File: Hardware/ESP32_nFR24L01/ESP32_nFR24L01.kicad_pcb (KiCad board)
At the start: 2 copper layers, 4 parts, among them J1 Conn_01x02_Female, U1 ESP32_DevKit_V1_DOIT, U2 NRF24L01_Breakout, U3 LM2596-Baja

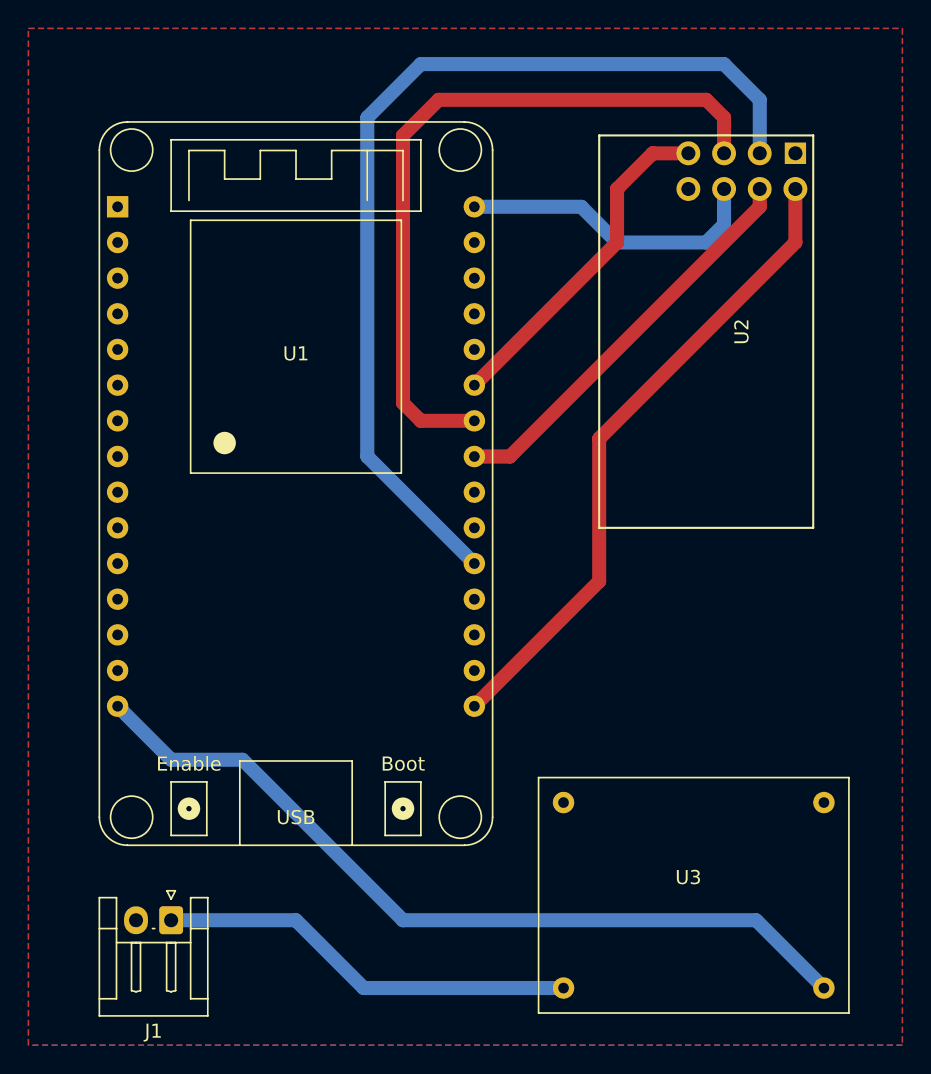
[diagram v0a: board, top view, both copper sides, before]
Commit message: Add PCB outline
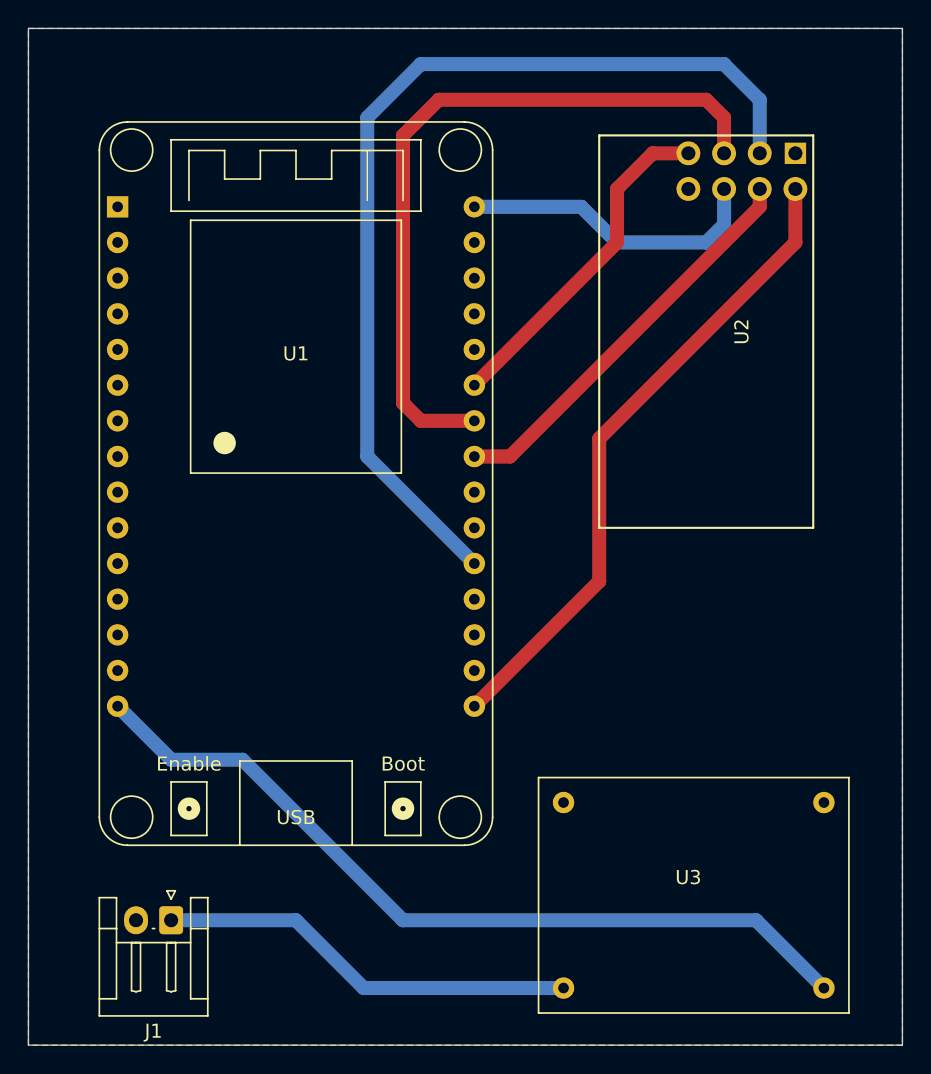
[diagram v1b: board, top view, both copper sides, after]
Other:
- board outline added: 62.2 x 72.4 mm
